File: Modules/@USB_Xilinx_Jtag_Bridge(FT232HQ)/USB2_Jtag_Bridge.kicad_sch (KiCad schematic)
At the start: 37 parts, among them J1 USB-C16PSMT01, J2 Conn_01x06_Male, U1 FT232H, U2 93LC56BxxOT, U3 mp9442, Y1 12M

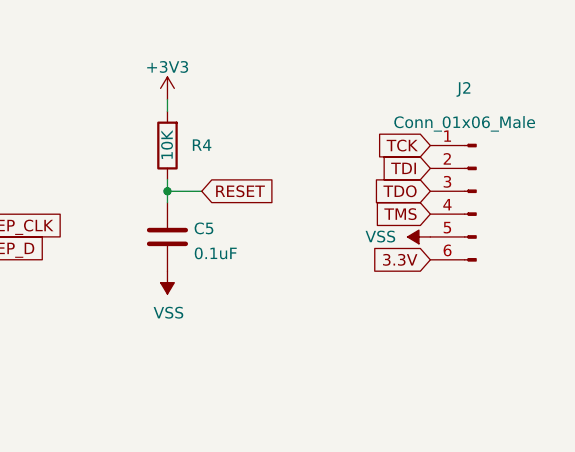
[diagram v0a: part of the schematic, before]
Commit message: Finish USB2_Jtag_Bridge
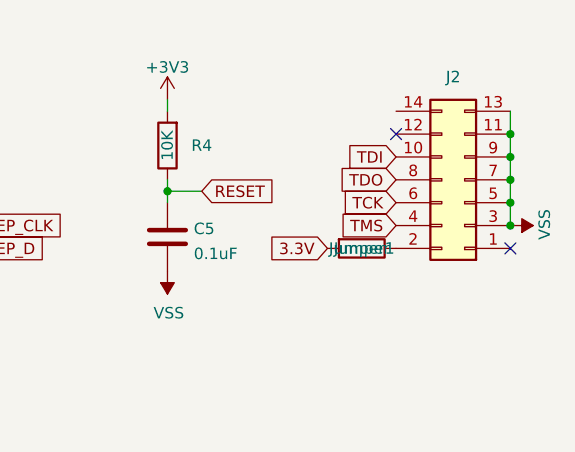
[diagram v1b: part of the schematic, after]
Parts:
- added Jumper1: Jumper, Resistor_SMD:R_0402_1005Metric, symbol Device:R
- J2: footprint Connector_PinHeader_2.54mm:PinHeader_1x06_P2.54mm_Vertical -> Connector_PinHeader_2.54mm:PinHeader_2x07_P2.54mm_Vertical; symbol Connector:Conn_01x06_Male -> Connector_Generic:Conn_02x07_Odd_Even
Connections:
- net 3.3V: now also Jumper1.2; no longer J2.6 (Pin_6)
- net TCK: now also J2.6 (Pin_6); no longer J2.1 (Pin_1)
- net TDI: now also J2.10 (Pin_10); no longer J2.2 (Pin_2)
- net TDO: now also J2.8 (Pin_8); no longer J2.3 (Pin_3)
- net VSS: now also J2.11 (Pin_11), J2.13 (Pin_13), J2.3 (Pin_3), J2.7 (Pin_7), J2.9 (Pin_9)
- new net: J2.2 (Pin_2), Jumper1.1
- no-connect marks 18 -> 20
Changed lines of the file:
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@@
   (junction (at 187.96 116.84) (diameter 0) (color 0 0 0 0)
   )
+  (junction (at 209.55 40.64) (diameter 0) (color 0 0 0 0)
+  )
   (junction (at 48.26 39.37) (diameter 0) (color 0 0 0 0)
   )
@@
   (junction (at 20.32 52.07) (diameter 0) (color 0 0 0 0)
   )
+  (junction (at 209.55 45.72) (diameter 0) (color 0 0 0 0)
+  )
   (junction (at 88.9 43.18) (diameter 0) (color 0 0 0 0)
   )
@@
   (junction (at 129.54 120.65) (diameter 0) (color 0 0 0 0)
   )
+  (junction (at 209.55 43.18) (diameter 0) (color 0 0 0 0)
+  )
   (junction (at 148.59 48.26) (diameter 0) (color 0 0 0 0)
   )
@@
   (junction (at 60.96 160.02) (diameter 0) (color 0 0 0 0)
   )
+  (junction (at 209.55 38.1) (diameter 0) (color 0 0 0 0)
+  )
   (junction (at 81.28 35.56) (diameter 0) (color 0 0 0 0)
   )
@@
   )
   (junction (at 78.74 160.02) (diameter 0) (color 0 0 0 0)
+  )
+  (junction (at 209.55 35.56) (diameter 0) (color 0 0 0 0)
   )
   (junction (at 63.5 160.02) (diameter 0) (color 0 0 0 0)
@@
   (no_connect (at 96.52 114.3))
   (no_connect (at 96.52 119.38))
+  (no_connect (at 209.55 48.26))
+  (no_connect (at 196.85 35.56))
   (no_connect (at 48.26 52.07))
   (no_connect (at 48.26 49.53))
@@
     (stroke (width 0) (type default) (color 0 0 0 0))
   )
+  (wire (pts (xy 209.55 35.56) (xy 209.55 33.02))
+    (stroke (width 0) (type default) (color 0 0 0 0))
+  )
+  (wire (pts (xy 209.55 40.64) (xy 209.55 38.1))
+    (stroke (width 0) (type default) (color 0 0 0 0))
+  )
   (wire (pts (xy 48.26 39.37) (xy 48.26 40.64))
     (stroke (width 0) (type default) (color 0 0 0 0))
@@
     (stroke (width 0) (type default) (color 0 0 0 0))
   )
+  (wire (pts (xy 209.55 45.72) (xy 209.55 43.18))
+    (stroke (width 0) (type default) (color 0 0 0 0))
+  )
   (wire (pts (xy 168.91 116.84) (xy 176.53 116.84))
     (stroke (width 0) (type default) (color 0 0 0 0))
@@
     (stroke (width 0) (type default) (color 0 0 0 0))
   )
+  (wire (pts (xy 209.55 38.1) (xy 209.55 35.56))
+    (stroke (width 0) (type default) (color 0 0 0 0))
+  )
   (wire (pts (xy 187.96 116.84) (xy 187.96 128.27))
     (stroke (width 0) (type default) (color 0 0 0 0))
@@
   )
   (wire (pts (xy 138.43 48.26) (xy 148.59 48.26))
+    (stroke (width 0) (type default) (color 0 0 0 0))
+  )
+  (wire (pts (xy 209.55 43.18) (xy 209.55 40.64))
     (stroke (width 0) (type default) (color 0 0 0 0))
   )
@@
     )
   )
-  (global_label "TMS" (shape input) (at 200.66 44.45 180) (fields_autoplaced)
+  (global_label "TMS" (shape input) (at 196.85 45.72 180) (fields_autoplaced)
     (effects (font (size 1.27 1.27)) (justify right))
-    (property "Intersheet References" "${INTERSHEET_REFS}" (id 0) (at 194.6183 44.3706 0)
+    (property "Intersheet References" "${INTERSHEET_REFS}" (id 0) (at 190.8083 45.7994 0)
       (effects (font (size 1.27 1.27)) (justify right) hide)
     )
@@
     )
   )
-  (global_label "TDO" (shape input) (at 200.66 41.91 180) (fields_autoplaced)
+  (global_label "TDO" (shape input) (at 196.85 40.64 180) (fields_autoplaced)
     (effects (font (size 1.27 1.27)) (justify right))
-    (property "Intersheet References" "${INTERSHEET_REFS}" (id 0) (at 194.6788 41.8306 0)
+    (property "Intersheet References" "${INTERSHEET_REFS}" (id 0) (at 190.8688 40.7194 0)
       (effects (font (size 1.27 1.27)) (justify right) hide)
     )
   )
-  (global_label "TDI" (shape input) (at 200.66 39.37 180) (fields_autoplaced)
+  (global_label "TDI" (shape input) (at 196.85 38.1 180) (fields_autoplaced)
     (effects (font (size 1.27 1.27)) (justify right))
-    (property "Intersheet References" "${INTERSHEET_REFS}" (id 0) (at 195.4045 39.2906 0)
+    (property "Intersheet References" "${INTERSHEET_REFS}" (id 0) (at 191.5945 38.1794 0)
       (effects (font (size 1.27 1.27)) (justify right) hide)
     )
@@
     )
   )
-  (global_label "TCK" (shape input) (at 200.66 36.83 180) (fields_autoplaced)
+  (global_label "TCK" (shape input) (at 196.85 43.18 180) (fields_autoplaced)
     (effects (font (size 1.27 1.27)) (justify right))
-    (property "Intersheet References" "${INTERSHEET_REFS}" (id 0) (at 194.7393 36.7506 0)
+    (property "Intersheet References" "${INTERSHEET_REFS}" (id 0) (at 190.9293 43.2594 0)
       (effects (font (size 1.27 1.27)) (justify right) hide)
     )
@@
     )
   )
-  (global_label "3.3V" (shape input) (at 200.66 49.53 180) (fields_autoplaced)
+  (global_label "3.3V" (shape input) (at 189.23 48.26 180) (fields_autoplaced)
     (effects (font (size 1.27 1.27)) (justify right))
-    (property "Intersheet References" "${INTERSHEET_REFS}" (id 0) (at 194.1345 49.6094 0)
+    (property "Intersheet References" "${INTERSHEET_REFS}" (id 0) (at 182.7045 48.1806 0)
       (effects (font (size 1.27 1.27)) (justify right) hide)
     )
@@
     (pin "2")
   )
-  (symbol (lib_id "Connector:Conn_01x06_Male") (at 205.74 41.91 0) (mirror y) (unit 1)
-    (in_bom yes) (on_board yes)
-    (property "Reference" "J2" (id 0) (at 204.47 30.48 0))
-    (property "Value" "Conn_01x06_Male" (id 1) (at 204.47 34.29 0))
-    (property "Footprint" "Connector_PinHeader_2.54mm:PinHeader_1x06_P2.54mm_Vertical" (id 2) (at 205.74 41.91 0)
-      (effects (font (size 1.27 1.27)) hide)
-    )
-    (property "Datasheet" "~" (id 3) (at 205.74 41.91 0)
-      (effects (font (size 1.27 1.27)) hide)
-    )
-    (pin "1")
+  (symbol (lib_id "Connector_Generic:Conn_02x07_Odd_Even") (at 204.47 40.64 180) (unit 1)
+    (in_bom yes) (on_board yes)
+    (property "Reference" "J2" (id 0) (at 203.2 29.21 0))
+    (property "Value" "Conn_01x06_Male" (id 1) (at 203.2 27.94 0)
+      (effects (font (size 1.27 1.27)) hide)
+    )
+    (property "Footprint" "Connector_PinHeader_2.54mm:PinHeader_2x07_P2.54mm_Vertical" (id 2) (at 204.47 40.64 0)
+      (effects (font (size 1.27 1.27)) hide)
+    )
+    (property "Datasheet" "~" (id 3) (at 204.47 40.64 0)
+      (effects (font (size 1.27 1.27)) hide)
+    )
+    (pin "1")
+    (pin "10")
+    (pin "11")
+    (pin "12")
+    (pin "13")
+    (pin "14")
     (pin "2")
     (pin "3")
@@
     (pin "5")
     (pin "6")
+    (pin "7")
+    (pin "8")
+    (pin "9")
   )
   (symbol (lib_id "Device:R") (at 46.99 119.38 270) (unit 1)
@@
     (pin "2")
   )
-  (symbol (lib_id "power:VSS") (at 200.66 46.99 90) (mirror x) (unit 1)
-    (in_bom yes) (on_board yes)
-    (property "Reference" "#PWR0114" (id 0) (at 204.47 46.99 0)
-      (effects (font (size 1.27 1.27)) hide)
-    )
-    (property "Value" "VSS" (id 1) (at 196.85 46.99 90)
-      (effects (font (size 1.27 1.27)) (justify left))
-    )
-    (property "Footprint" "" (id 2) (at 200.66 46.99 0)
-      (effects (font (size 1.27 1.27)) hide)
-    )
-    (property "Datasheet" "" (id 3) (at 200.66 46.99 0)
-      (effects (font (size 1.27 1.27)) hide)
-    )
-    (pin "1")
+  (symbol (lib_id "power:VSS") (at 209.55 45.72 270) (unit 1)
+    (in_bom yes) (on_board yes)
+    (property "Reference" "#PWR0114" (id 0) (at 205.74 45.72 0)
+      (effects (font (size 1.27 1.27)) hide)
+    )
+    (property "Value" "VSS" (id 1) (at 213.3579 43.8977 0)
+      (effects (font (size 1.27 1.27)) (justify left))
+    )
+    (property "Footprint" "" (id 2) (at 209.55 45.72 0)
+      (effects (font (size 1.27 1.27)) hide)
+    )
+    (property "Datasheet" "" (id 3) (at 209.55 45.72 0)
+      (effects (font (size 1.27 1.27)) hide)
+    )
+    (pin "1")
+  )
+  (symbol (lib_id "Device:R") (at 193.04 48.26 270) (unit 1)
+    (in_bom yes) (on_board yes)
+    (property "Reference" "Jumper1" (id 0) (at 193.04 48.26 90))
+    (property "Value" "Jumper" (id 1) (at 193.04 48.26 90))
+    (property "Footprint" "Resistor_SMD:R_0402_1005Metric" (id 2) (at 193.04 46.482 90)
+      (effects (font (size 1.27 1.27)) hide)
+    )
+    (property "Datasheet" "~" (id 3) (at 193.04 48.26 0)
+      (effects (font (size 1.27 1.27)) hide)
+    )
+    (pin "1")
+    (pin "2")
   )
   (symbol (lib_id "Device:LED") (at 138.43 120.65 0) (unit 1)
@@
     )
     (path "/4588f9bf-86ea-477c-b187-a5130533b265"
-      (reference "J2") (unit 1) (value "Conn_01x06_Male") (footprint "Connector_PinHeader_2.54mm:PinHeader_1x06_P2.54mm_Vertical")
+      (reference "J2") (unit 1) (value "Conn_01x06_Male") (footprint "Connector_PinHeader_2.54mm:PinHeader_2x07_P2.54mm_Vertical")
+    )
+    (path "/9486eaf1-02fa-4cbc-9ed7-eb03d1bc9760"
+      (reference "Jumper1") (unit 1) (value "Jumper") (footprint "Resistor_SMD:R_0402_1005Metric")
     )
     (path "/10188ce2-15ce-40e2-97b0-6def54704842"

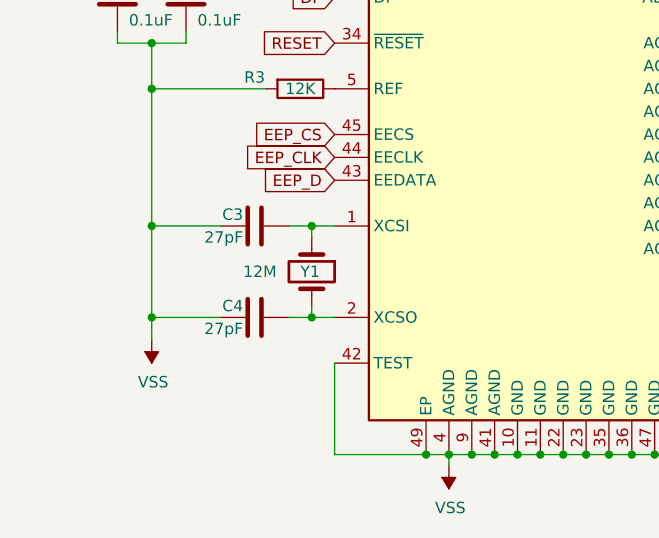
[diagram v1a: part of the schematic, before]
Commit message: Crystal footprint fix
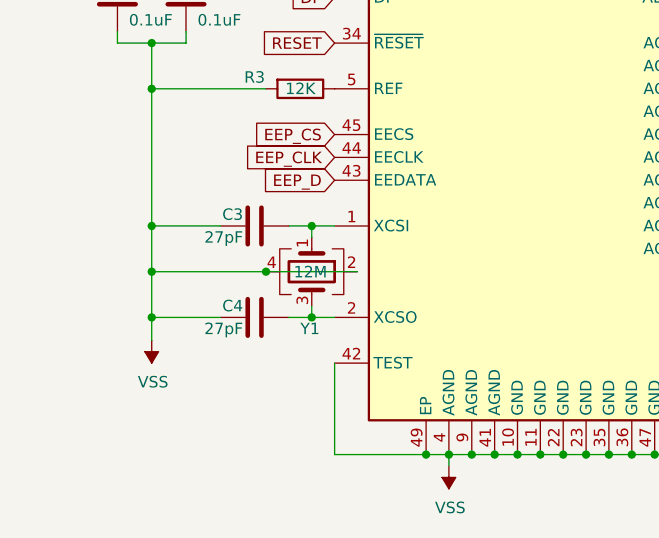
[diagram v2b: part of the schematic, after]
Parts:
- Y1: footprint Crystal:Crystal_SMD_TXC_9HT11-2Pin_2.0x1.2mm_HandSoldering -> Crystal:Crystal_SMD_2016-4Pin_2.0x1.6mm; symbol Device:Crystal -> Device:Crystal_GND24
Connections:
- net VSS: now also Y1.2, Y1.4
- net at C4.2, U1.2 (XCSO): now also Y1.3; no longer Y1.2
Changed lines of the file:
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@@
 (kicad_sch (version 20211123) (generator eeschema)
   (paper "User" 231.8 209.398)
+  (junction (at 30.48 139.7) (diameter 0) (color 0 0 0 0)
+  )
   (junction (at 48.26 144.78) (diameter 0) (color 0 0 0 0)
   )
@@
   )
   (junction (at 116.84 45.72) (diameter 0) (color 0 0 0 0)
+  )
+  (junction (at 43.18 139.7) (diameter 0) (color 0 0 0 0)
   )
   (junction (at 142.24 120.65) (diameter 0) (color 0 0 0 0)
@@
     (stroke (width 0) (type default) (color 0 0 0 0))
   )
+  (wire (pts (xy 30.48 139.7) (xy 43.18 139.7))
+    (stroke (width 0) (type default) (color 0 0 0 0))
+  )
   (wire (pts (xy 48.26 135.89) (xy 48.26 134.62))
     (stroke (width 0) (type default) (color 0 0 0 0))
@@
     (stroke (width 0) (type default) (color 0 0 0 0))
   )
+  (wire (pts (xy 43.18 139.7) (xy 53.34 139.7))
+    (stroke (width 0) (type default) (color 0 0 0 0))
+  )
   (wire (pts (xy 81.28 160.02) (xy 83.82 160.02))
     (stroke (width 0) (type default) (color 0 0 0 0))
@@
     (stroke (width 0) (type default) (color 0 0 0 0))
   )
-  (wire (pts (xy 30.48 134.62) (xy 30.48 144.78))
+  (wire (pts (xy 30.48 134.62) (xy 30.48 139.7))
     (stroke (width 0) (type default) (color 0 0 0 0))
   )
@@
   )
   (wire (pts (xy 81.28 43.18) (xy 85.09 43.18))
+    (stroke (width 0) (type default) (color 0 0 0 0))
+  )
+  (wire (pts (xy 30.48 139.7) (xy 30.48 144.78))
     (stroke (width 0) (type default) (color 0 0 0 0))
   )
@@
     (pin "1")
   )
-  (symbol (lib_id "Device:Crystal") (at 48.26 139.7 270) (unit 1)
-    (in_bom yes) (on_board yes)
-    (property "Reference" "Y1" (id 0) (at 46.99 139.7 90)
-      (effects (font (size 1.27 1.27)) (justify left))
-    )
-    (property "Value" "12M" (id 1) (at 40.64 139.7 90)
-      (effects (font (size 1.27 1.27)) (justify left))
-    )
-    (property "Footprint" "Crystal:Crystal_SMD_TXC_9HT11-2Pin_2.0x1.2mm_HandSoldering" (id 2) (at 48.26 139.7 0)
+  (symbol (lib_id "Device:Crystal_GND24") (at 48.26 139.7 270) (unit 1)
+    (in_bom yes) (on_board yes)
+    (property "Reference" "Y1" (id 0) (at 46.99 146.05 90)
+      (effects (font (size 1.27 1.27)) (justify left))
+    )
+    (property "Value" "12M" (id 1) (at 46.2597 139.7433 90)
+      (effects (font (size 1.27 1.27)) (justify left))
+    )
+    (property "Footprint" "Crystal:Crystal_SMD_2016-4Pin_2.0x1.6mm" (id 2) (at 48.26 139.7 0)
       (effects (font (size 1.27 1.27)) hide)
     )
@@
     (pin "1")
     (pin "2")
+    (pin "3")
+    (pin "4")
   )
   (symbol (lib_id "power:VSS") (at 133.35 27.94 0) (mirror y) (unit 1)
@@
     )
     (path "/2c53b288-efa2-43e5-988d-4c69e327d17f"
-      (reference "Y1") (unit 1) (value "12M") (footprint "Crystal:Crystal_SMD_TXC_9HT11-2Pin_2.0x1.2mm_HandSoldering")
-    )
-  )
+      (reference "Y1") (unit 1) (value "12M") (footprint "Crystal:Crystal_SMD_2016-4Pin_2.0x1.6mm")
+    )
+  )
